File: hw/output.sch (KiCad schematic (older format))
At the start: 43 parts, among them J401 Conn_01x02, J402 Conn_01x02, J403 Conn_01x02, J404 HC_OUT, J405 Conn_01x02, J406 Conn_01x02, J407 Conn_01x02, J409 ServoCon, J410 AUDIO, Q401 IRLML6344TRPBF, Q402 IRLML6344TRPBF, Q403 IRLML6344TRPBF, Q404 CSD17306Q5A, Q406 IRLML6344TRPBF, Q408 CSD17306Q5A, U401 MCP1416, U402 MCP1416, U403 AD5160BRJZ10-R2, U404 MCP6001-OT, U405 TLP2361_TPL_E, U406 TLP2361_TPL_E

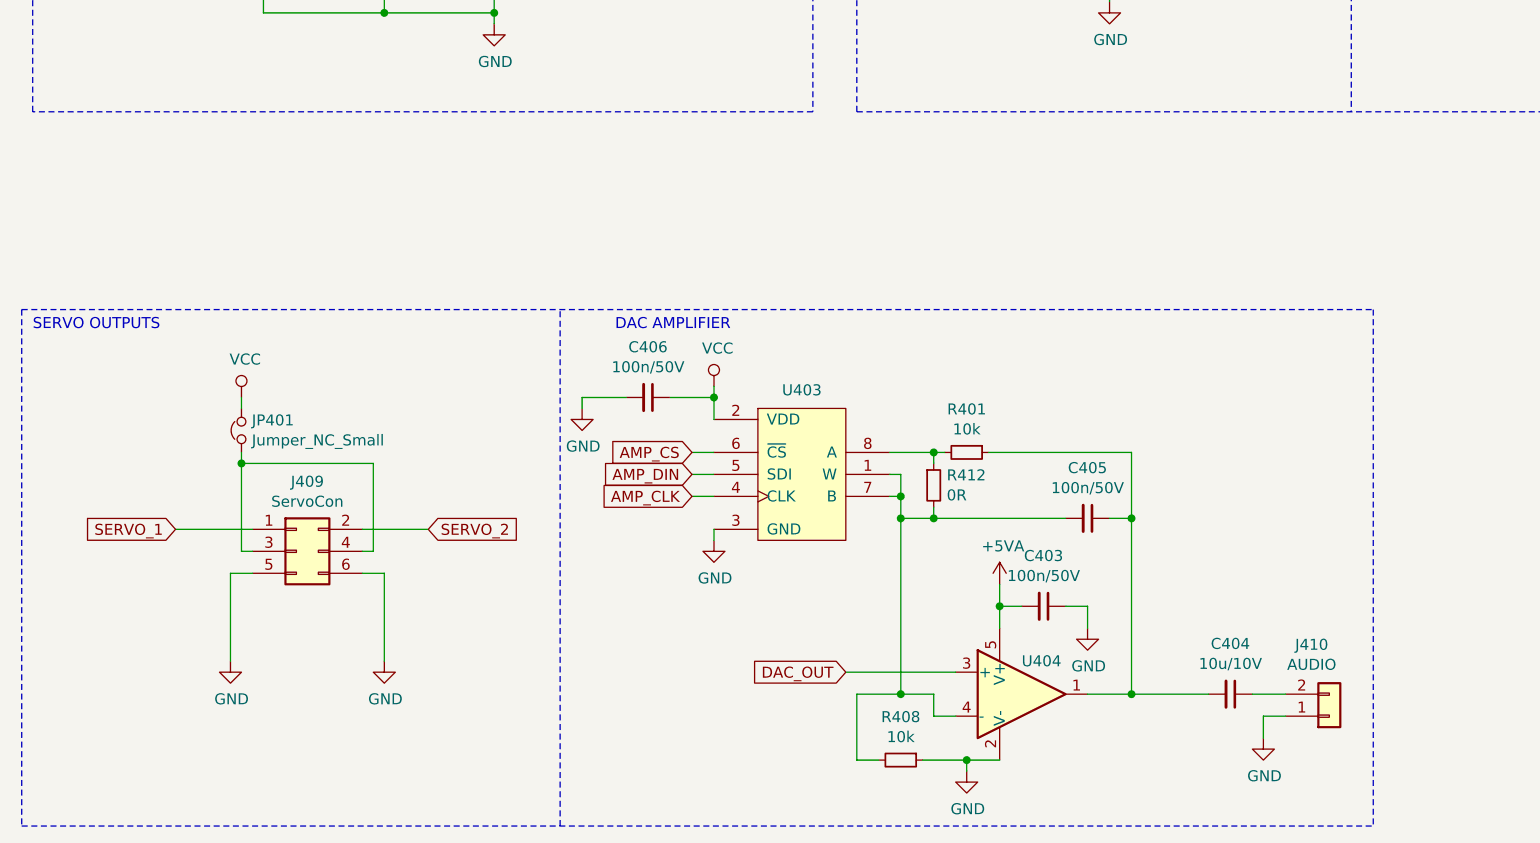
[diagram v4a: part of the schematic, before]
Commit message: DAC Amplifier improvements
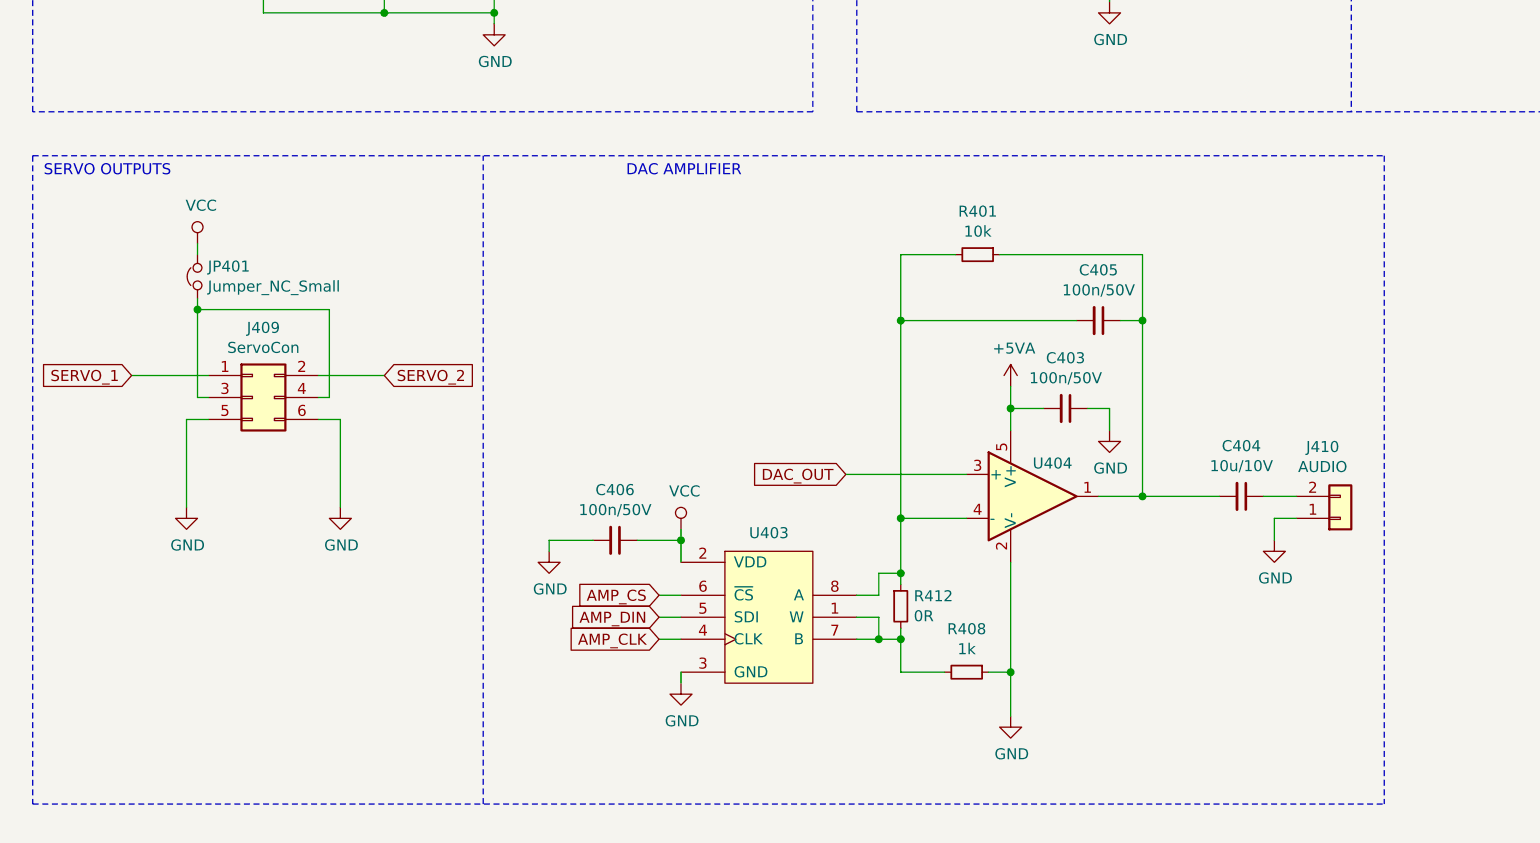
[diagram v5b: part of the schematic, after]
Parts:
- R408: value 10k -> 1k
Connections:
- net at R408.2, R412.2, U403.1 (W)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: no longer C405.2, U404.4 (-)
- net at R401.2, R412.1, U403.8 (A): now also C405.2, U404.4 (-)
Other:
- moved on the sheet: C403, C404, C405, C406, J409, J410, JP401, R401, R412, U403, U404

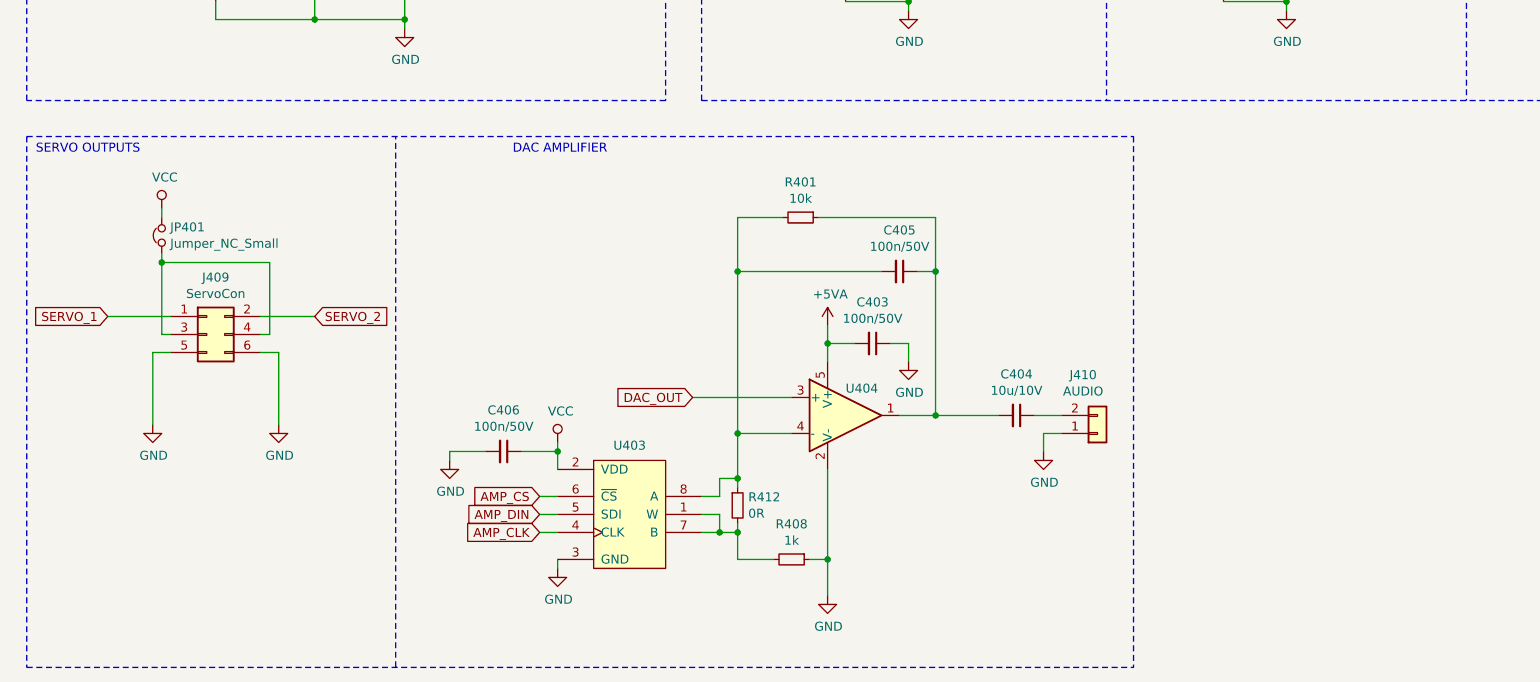
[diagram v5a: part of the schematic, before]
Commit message: Added additional opamp to DAC output as a buffer.
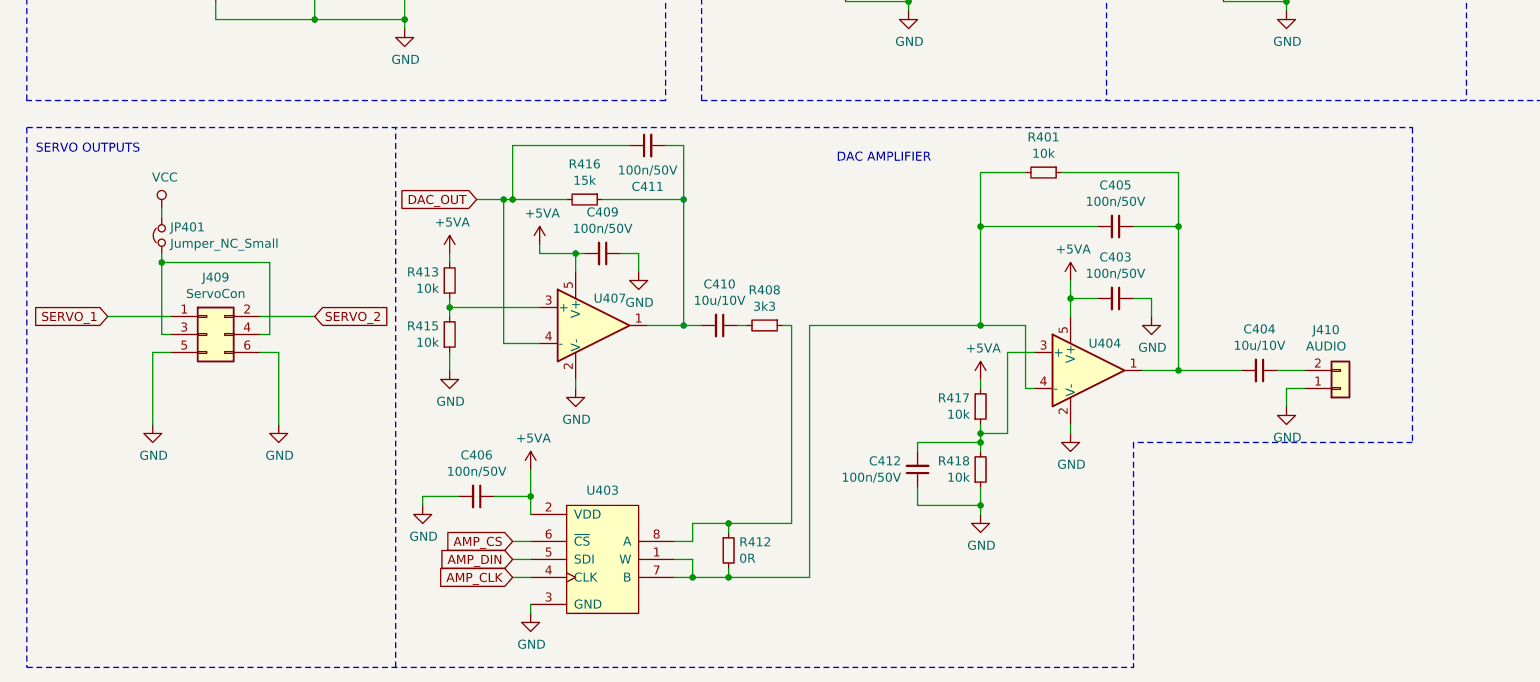
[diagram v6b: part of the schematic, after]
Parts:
- added C409, C411, C412: 100n/50V, Capacitor_SMD:C_0603_1608Metric_Pad1.05x0.95mm_HandSolder, symbol Device:C_Small
- added C410: 10u/10V, Capacitor_SMD:C_0603_1608Metric_Pad1.05x0.95mm_HandSolder, symbol Device:C_Small
- added R413, R415, R417, R418: 10k, Resistor_SMD:R_0603_1608Metric_Pad1.05x0.95mm_HandSolder, symbol Device:R_Small
- added R416: 15k, Resistor_SMD:R_0603_1608Metric_Pad1.05x0.95mm_HandSolder, symbol Device:R_Small
- added U407: MCP6001-OT, Package_TO_SOT_SMD:SOT-23-5_HandSoldering, symbol Amplifier_Operational:MCP6001-OT
- J404: Config (none) -> -prod
- R408: value 1k -> 3k3
- U401, U402, U404: footprint TO_SOT_Packages_SMD:SOT-23-5_HandSoldering -> Package_TO_SOT_SMD:SOT-23-5_HandSoldering
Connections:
- net +5VA: now also C406.1, U403.2 (VDD), C409.2, R413.2, R417.2, U407.5 (V+)
- net DAC_OUT: now also C411.1, R416.2, U407.4 (-); no longer U404.3 (+)
- net GND: now also C409.1, C412.1, R415.1, R418.1, U407.2 (V-); no longer R408.1
- net VCC: no longer C406.1, U403.2 (VDD)
- net at C405.2, R401.2, U404.4 (-): now also R412.2, U403.1 (W), U403.7 (B); no longer R412.1, U403.8 (A)
- new net: C412.2, R417.1, R418.2, U404.3 (+)
- new net: R408.1, R412.1, U403.8 (A)
- new net: C410.2, C411.2, R416.1, U407.1
- new net: R413.1, R415.2, U407.3 (+)
- new net: C410.1, R408.2
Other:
- moved on the sheet: C403, C404, C405, C406, J410, R401, R408, R412, U403, U404

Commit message: Signal remapping for Flash Memory and component optimizations
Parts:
- R401: value 10k -> 15k
- R402, R403, R404, R410: value 10 -> 1k5
- R405, R406, R407, R414: value 10k -> 75k
- R408: value 3k3 -> 6k2
- R409, R411: value 100 -> 1k5
- U401, U402: symbol Telemetry-rescue:MCP1416-Driver_FET -> Telemetry-rescue:MCP1416-Driver_FET-Telemetry-rescue
- U403: symbol Telemetry-rescue:AD5160BRJZ10-R2-Misc -> Telemetry-rescue:AD5160BRJZ10-R2-Misc-Telemetry-rescue
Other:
- note added: "OPTO INPUTS \nMaximum input voltage 15 V"
- note removed: "OPTO INPUTS"
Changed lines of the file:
@@
 P 5150 2000
 F 0 "R405" H 5091 1954 50  0000 R CNN
-F 1 "10k" H 5091 2045 50  0000 R CNN
+F 1 "75k" H 5091 2045 50  0000 R CNN
 F 2 "Resistor_SMD:R_0603_1608Metric_Pad1.05x0.95mm_HandSolder" H 5150 2000 50  0001 C CNN
 F 3 "~" H 5150 2000 50  0001 C CNN
@@
 P 5000 1800
 F 0 "R402" V 4804 1800 50  0000 C CNN
-F 1 "10" V 4895 1800 50  0000 C CNN
+F 1 "1k5" V 4895 1800 50  0000 C CNN
 F 2 "Resistor_SMD:R_0603_1608Metric_Pad1.05x0.95mm_HandSolder" H 5000 1800 50  0001 C CNN
 F 3 "~" H 5000 1800 50  0001 C CNN
@@
 P 7100 1800
 F 0 "R403" V 6904 1800 50  0000 C CNN
-F 1 "10" V 6995 1800 50  0000 C CNN
+F 1 "1k5" V 6995 1800 50  0000 C CNN
 F 2 "Resistor_SMD:R_0603_1608Metric_Pad1.05x0.95mm_HandSolder" H 7100 1800 50  0001 C CNN
 F 3 "~" H 7100 1800 50  0001 C CNN
@@
 $EndComp
 $Comp
-L Telemetry-rescue:MCP1416-Driver_FET U402
+L Telemetry-rescue:MCP1416-Driver_FET-Telemetry-rescue U402
 U 1 1 5CEC7B81
 P 1650 3650
@@
 Connection ~ 2700 2950
 $Comp
-L Telemetry-rescue:MCP1416-Driver_FET U401
+L Telemetry-rescue:MCP1416-Driver_FET-Telemetry-rescue U401
 U 1 1 5CED0BC8
 P 1700 1800
@@
 P 6250 4900
 F 0 "R401" V 6054 4900 50  0000 C CNN
-F 1 "10k" V 6145 4900 50  0000 C CNN
+F 1 "15k" V 6145 4900 50  0000 C CNN
 F 2 "Resistor_SMD:R_0603_1608Metric_Pad1.05x0.95mm_HandSolder" H 6250 4900 50  0001 C CNN
 F 3 "~" H 6250 4900 50  0001 C CNN
@@
 SERVO OUTPUTS
 $Comp
-L Telemetry-rescue:AD5160BRJZ10-R2-Misc U403
+L Telemetry-rescue:AD5160BRJZ10-R2-Misc-Telemetry-rescue U403
 U 1 1 5CEF134B
 P 3800 7000
+AR Path="/5CEF134B" Ref="U403"  Part="1"
+AR Path="/5CEA3FFC/5CEF134B" Ref="U403"  Part="1"
 F 0 "U403" H 3800 7333 50  0000 C CNN
 F 1 "AD5160BRJZ10-R2" H 3800 7400 50  0001 C CNN
@@
 P 9550 3300
 F 0 "R411" V 9354 3300 50  0000 C CNN
-F 1 "100" V 9445 3300 50  0000 C CNN
+F 1 "1k5" V 9445 3300 50  0000 C CNN
 F 2 "Resistor_SMD:R_0603_1608Metric_Pad1.05x0.95mm_HandSolder" H 9550 3300 50  0001 C CNN
 F 3 "~" H 9550 3300 50  0001 C CNN
@@
 P 9550 1600
 F 0 "R409" V 9354 1600 50  0000 C CNN
-F 1 "100" V 9445 1600 50  0000 C CNN
+F 1 "1k5" V 9445 1600 50  0000 C CNN
 F 2 "Resistor_SMD:R_0603_1608Metric_Pad1.05x0.95mm_HandSolder" H 9550 1600 50  0001 C CNN
 F 3 "~" H 9550 1600 50  0001 C CNN
@@
 Wire Notes Line
 	11000 4500 11000 650
-Text Notes 8650 750  0    50   ~ 0
-OPTO INPUTS
+Text Notes 8650 850  0    50   ~ 0
+OPTO INPUTS \nMaximum input voltage 15 V
 Wire Wire Line
 	9400 3500 9800 3500
@@
 P 7250 2000
 F 0 "R406" H 7191 1954 50  0000 R CNN
-F 1 "10k" H 7191 2045 50  0000 R CNN
+F 1 "75k" H 7191 2045 50  0000 R CNN
 F 2 "Resistor_SMD:R_0603_1608Metric_Pad1.05x0.95mm_HandSolder" H 7250 2000 50  0001 C CNN
 F 3 "~" H 7250 2000 50  0001 C CNN
@@
 P 7100 3650
 F 0 "R404" V 6904 3650 50  0000 C CNN
-F 1 "10" V 6995 3650 50  0000 C CNN
+F 1 "1k5" V 6995 3650 50  0000 C CNN
 F 2 "Resistor_SMD:R_0603_1608Metric_Pad1.05x0.95mm_HandSolder" H 7100 3650 50  0001 C CNN
 F 3 "~" H 7100 3650 50  0001 C CNN
@@
 P 5000 3650
 F 0 "R410" V 4804 3650 50  0000 C CNN
-F 1 "10" V 4895 3650 50  0000 C CNN
+F 1 "1k5" V 4895 3650 50  0000 C CNN
 F 2 "Resistor_SMD:R_0603_1608Metric_Pad1.05x0.95mm_HandSolder" H 5000 3650 50  0001 C CNN
 F 3 "~" H 5000 3650 50  0001 C CNN
@@
 P 5150 3850
 F 0 "R414" H 5091 3804 50  0000 R CNN
-F 1 "10k" H 5091 3895 50  0000 R CNN
+F 1 "75k" H 5091 3895 50  0000 R CNN
 F 2 "Resistor_SMD:R_0603_1608Metric_Pad1.05x0.95mm_HandSolder" H 5150 3850 50  0001 C CNN
 F 3 "~" H 5150 3850 50  0001 C CNN
@@
 P 7250 3850
 F 0 "R407" H 7191 3804 50  0000 R CNN
-F 1 "10k" H 7191 3895 50  0000 R CNN
+F 1 "75k" H 7191 3895 50  0000 R CNN
 F 2 "Resistor_SMD:R_0603_1608Metric_Pad1.05x0.95mm_HandSolder" H 7250 3850 50  0001 C CNN
 F 3 "~" H 7250 3850 50  0001 C CNN
@@
 P 4700 5750
 F 0 "R408" V 4504 5750 50  0000 C CNN
-F 1 "3k3" V 4595 5750 50  0000 C CNN
+F 1 "6k2" V 4595 5750 50  0000 C CNN
 F 2 "Resistor_SMD:R_0603_1608Metric_Pad1.05x0.95mm_HandSolder" H 4700 5750 50  0001 C CNN
 F 3 "~" H 4700 5750 50  0001 C CNN

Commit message: Design updates
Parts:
- JP401: footprint Connector_PinHeader_2.54mm:PinHeader_1x02_P2.54mm_Vertical -> Connector_PinHeader_1.27mm:PinHeader_1x02_P1.27mm_Vertical
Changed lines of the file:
@@
 F 0 "JP401" V 1396 5203 50  0000 R CNN
 F 1 "Jumper_NC_Small" V 1305 5203 50  0000 R CNN
-F 2 "Connector_PinHeader_2.54mm:PinHeader_1x02_P2.54mm_Vertical" H 1350 5250 50  0001 C CNN
+F 2 "Connector_PinHeader_1.27mm:PinHeader_1x02_P1.27mm_Vertical" H 1350 5250 50  0001 C CNN
 F 3 "~" H 1350 5250 50  0001 C CNN
 F 4 "-prod" H 1350 5250 50  0001 C CNN "Config"
